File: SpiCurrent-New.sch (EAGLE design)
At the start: 32 parts, among them IC1 AD822N, Q1 IRFB4610, Q2 IRFB4610, Q3 IRFB4610, Q4 IRFB4610, U1 HIP4081AIPZ

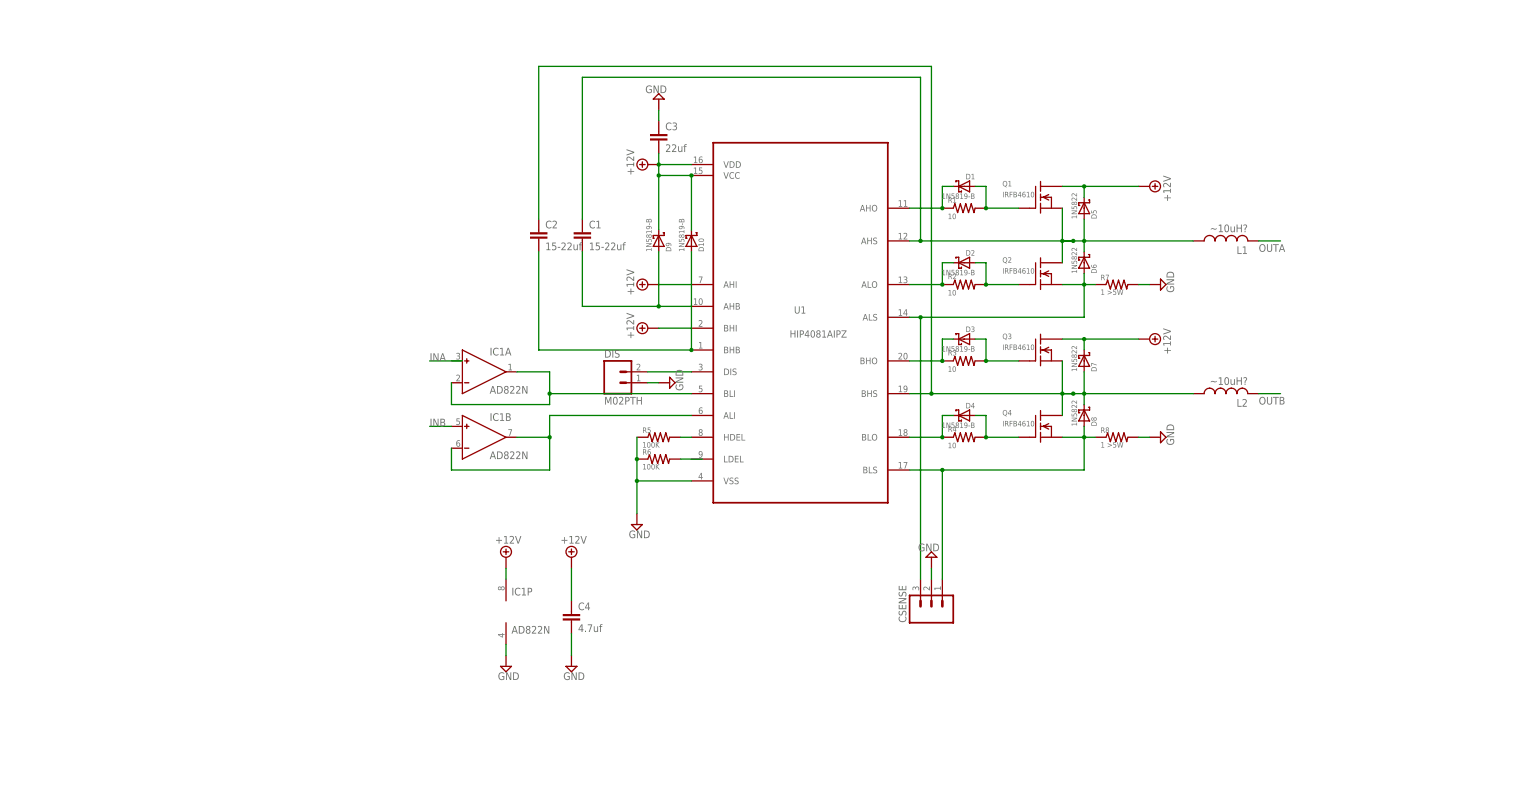
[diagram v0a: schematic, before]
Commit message: Added MCU and hall effect sensor
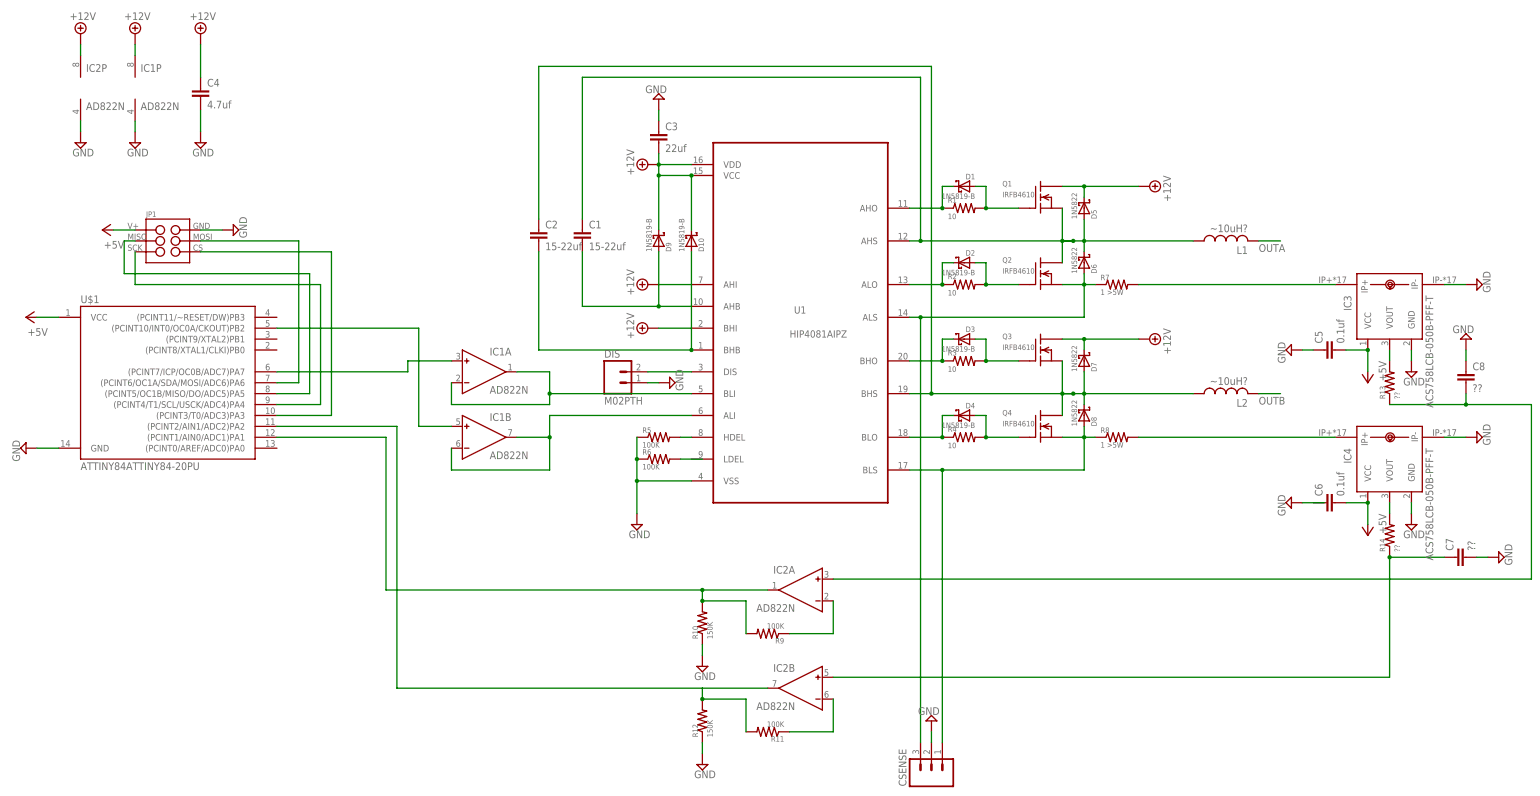
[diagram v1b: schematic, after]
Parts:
- added C5, C6: 0.1uf, rcl:C-EU050-055X075
- added C7, C8: ??, rcl:C-EU050-055X075
- added IC2: AD822N, analog-devices:AD822N
- added IC3, IC4: ACS758LCB-050B-PFF-T, allegro:ACS758LCB-050B-PFF-T
- added JP1: (no value), CustomParts:M03X2SHROUD
- added R10, R12: 150K, resistor-custom:R-US_0207/10
- added R11, R9: 100K, resistor-custom:R-US_0207/10
- added R13, R14: ??, resistor-custom:R-US_0207/10
- added U$1: ATTINY84ATTINY84-20PU, SparkFun-DigitalIC:ATTINY84ATTINY84-20PU
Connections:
- removed net INB: IC1B.IN+
- new net +5V: C5.2, C6.2, IC3.VCC, IC4.VCC, JP1.1, U$1.VCC
- new net N$20: JP1.4, U$1.(PCINT6/OC1A/SDA/MOSI/ADC6)PA6
- new net N$21: JP1.3, U$1.(PCINT5/OC1B/MISO/DO/ADC5)PA5
- new net N$22: JP1.5, U$1.(PCINT4/T1/SCL/USCK/ADC4)PA4
- new net N$23: JP1.6, U$1.(PCINT3/T0/ADC3)PA3
- new net N$24: IC1B.IN+, U$1.(PCINT10/INT0/OC0A/CKOUT)PB2
- new net N$25: IC1A.IN+, U$1.(PCINT7/ICP/OC0B/ADC7)PA7
- new net N$26: IC2A.IN-, R9.1
- new net N$27: IC4.IP+, R8.2
- new net N$28: IC2A.OUT, R10.2, R9.2, U$1.(PCINT1/AIN0/ADC1)PA1
- new net N$29: IC2B.OUT, R11.2, R12.2, U$1.(PCINT2/AIN1/ADC2)PA2
- new net N$30: IC2B.IN-, R11.1
- new net N$31: IC3.IP+, R7.2
- new net N$32: C8.2, IC2A.IN+, R13.1
- new net N$33: C7.1, IC2B.IN+, R14.1
- new net N$34: IC3.VOUT, R13.2
- new net N$35: IC4.VOUT, R14.2
- net +12V: now also IC2P.V+
- net GND: now also C5.1, C7.2, C8.1, IC2P.V-, IC3.GND, IC3.IP-, IC4.GND, IC4.IP-, JP1.2, R10.1, R12.1, U$1.GND; no longer R7.2, R8.2
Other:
- moved on the sheet: C4, CSENSE, IC1P
